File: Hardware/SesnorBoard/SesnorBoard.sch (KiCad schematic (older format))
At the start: 31 parts, among them J1 Mainboard connection, J2 microphoon connection, U1 AMG8833, U2 CCS811, U3 NC7SVU04P5X

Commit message: updated the sensor part of the report and corrected some issues of the PCB design.
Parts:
- J2: footprint Connector_PinHeader_2.00mm:PinHeader_1x03_P2.00mm_Vertical -> Connector_PinHeader_2.54mm:PinHeader_1x03_P2.54mm_Vertical
- R21: value 100k -> 1M
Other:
- note added: "Tau = 10 ms"
- note removed: "Tau = 1 ms"
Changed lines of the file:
@@
 F 0 "J2" H 1868 3575 50  0000 C CNN
 F 1 "microphoon connection" H 1868 3666 50  0000 C CNN
-F 2 "Connector_PinHeader_2.00mm:PinHeader_1x03_P2.00mm_Vertical" H 1950 3900 50  0001 C CNN
+F 2 "Connector_PinHeader_2.54mm:PinHeader_1x03_P2.54mm_Vertical" H 1950 3900 50  0001 C CNN
 F 3 "~" H 1950 3900 50  0001 C CNN
 	1    1950 3900
@@
 $EndComp
 Connection ~ 3100 5100
-Text Label 2150 4600 0    50   ~ 0
-AUDIO_OUT
 Text Label 3950 4600 2    50   ~ 0
 DETECTOR_OUT
 Wire Wire Line
 	3950 4600 3300 4600
-Wire Wire Line
-	2700 4600 2150 4600
 Connection ~ 3300 4600
 Wire Wire Line
@@
 	3100 4600 3100 4700
 Text Notes 2500 5050 0    50   ~ 0
-Tau = 1 ms
+Tau = 10 ms
 Wire Notes Line
 	4200 5650 4200 3300
@@
 P 3300 4850
 F 0 "R21" H 3300 4950 50  0000 C CNN
-F 1 "100k" H 3300 4850 40  0000 C CNB
+F 1 "1M" H 3300 4850 40  0000 C CNB
 F 2 "Resistor_SMD:R_1206_3216Metric" H 3300 4850 50  0001 C CNN
 F 3 "" H 3300 4850 50  0001 C CNN
@@
 Wire Wire Line
 	1100 2550 2050 2550
+Text Label 2150 4600 0    50   ~ 0
+AUDIO_OUT
+Wire Wire Line
+	2700 4600 2150 4600
 $EndSCHEMATC

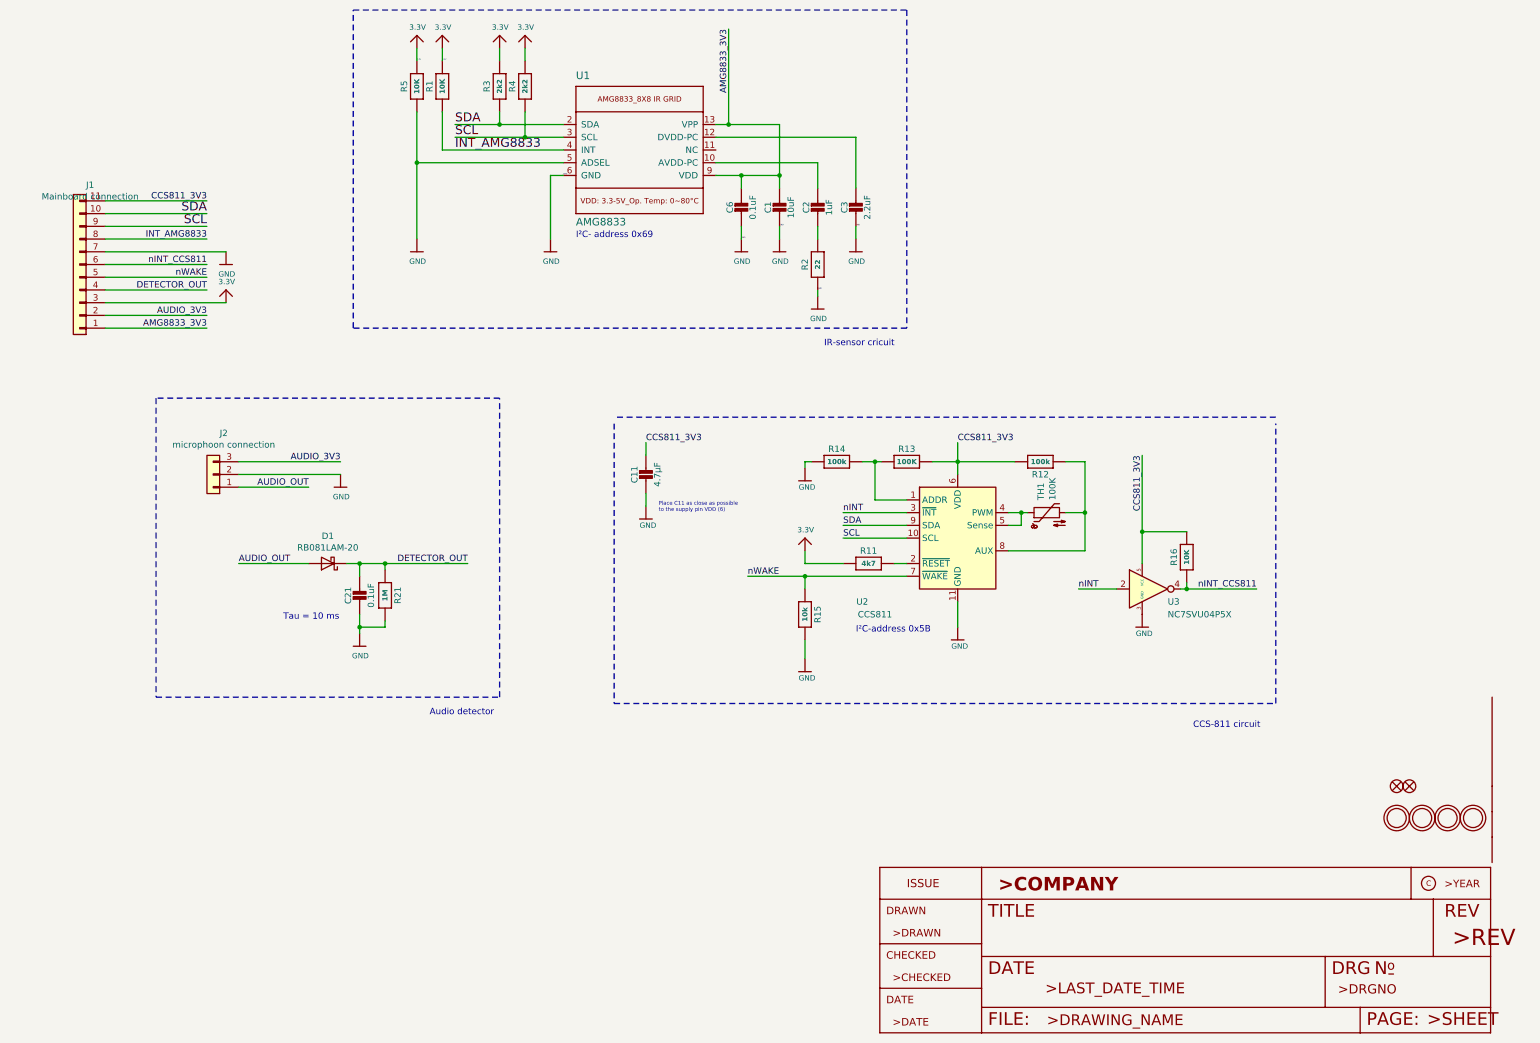
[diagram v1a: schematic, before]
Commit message: Figures added sensor part in report
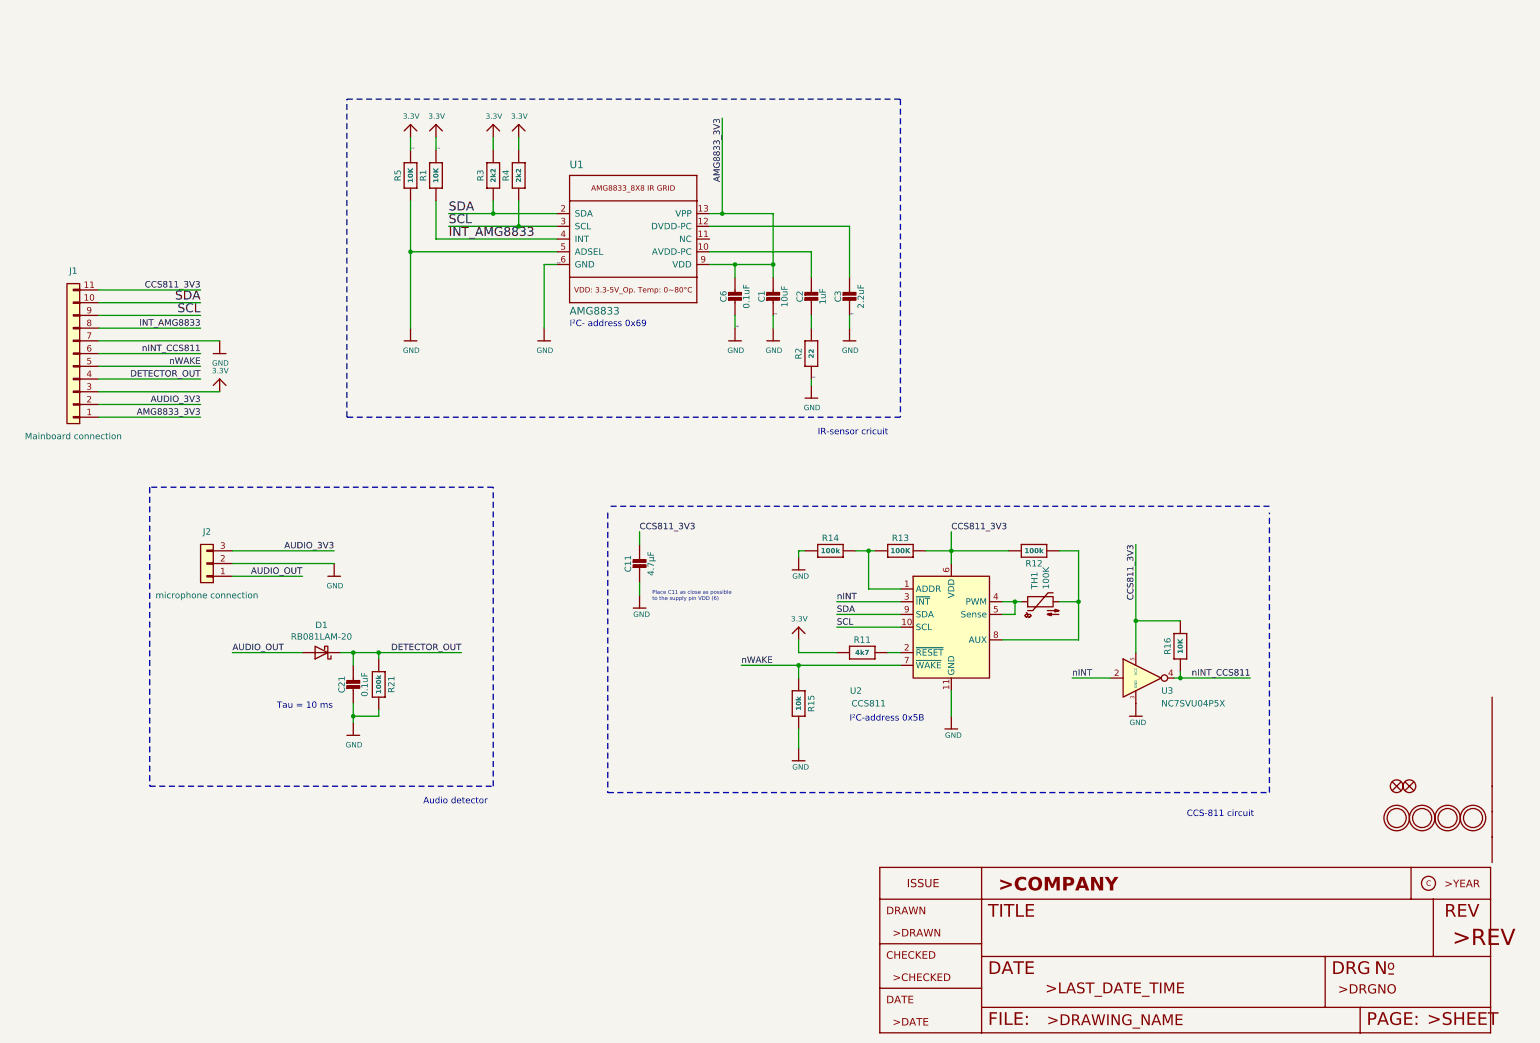
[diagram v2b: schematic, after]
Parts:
- J2: value microphoon connection -> microphone connection
- R21: value 1M -> 100k
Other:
- moved on the sheet: C1, C11, C2, C21, C3, C6, D1, J1, J2, R1, R11, R12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
